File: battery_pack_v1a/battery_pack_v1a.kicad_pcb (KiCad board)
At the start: 4 copper layers, 88 x 94.5 mm, 26 parts, among them J1 Battery Input, Q1 IRF7458, Q2 IRF7458, U1 R5460N208AA

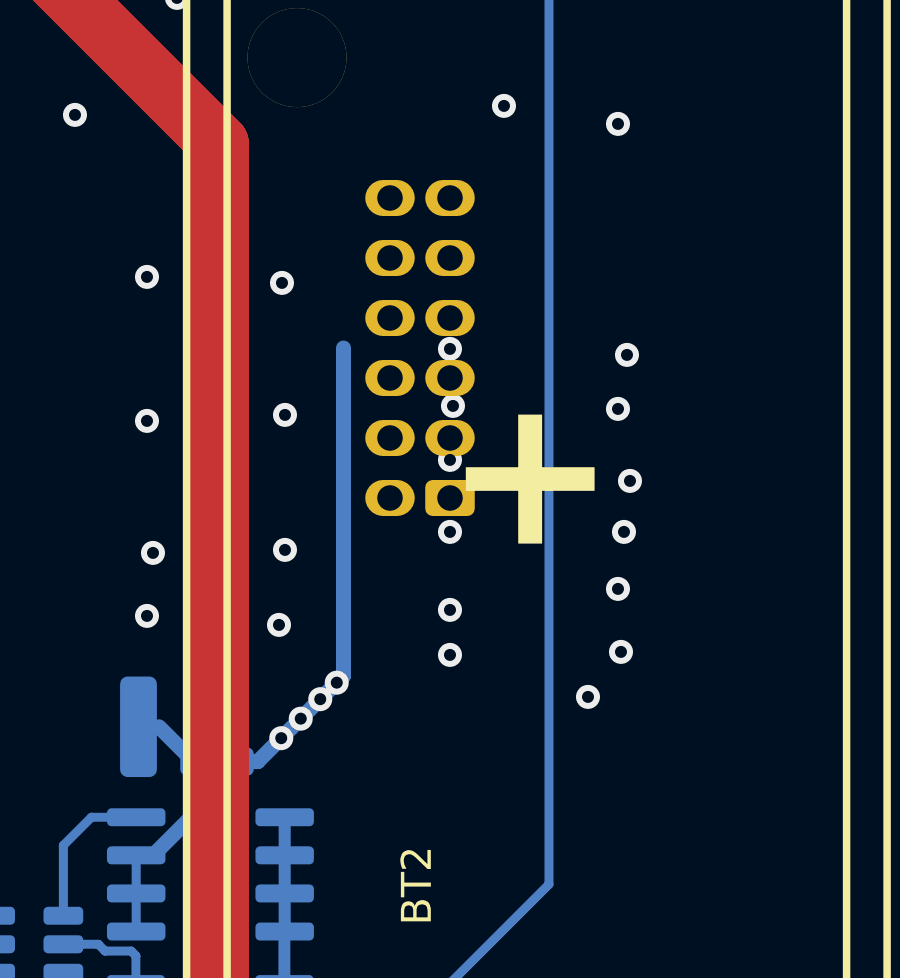
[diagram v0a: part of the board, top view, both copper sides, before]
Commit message: Fixed DF11 footprint and added new (working) repo
Working repo is pack_v1a (ignore pack_v1, will restore original version later in this branch)
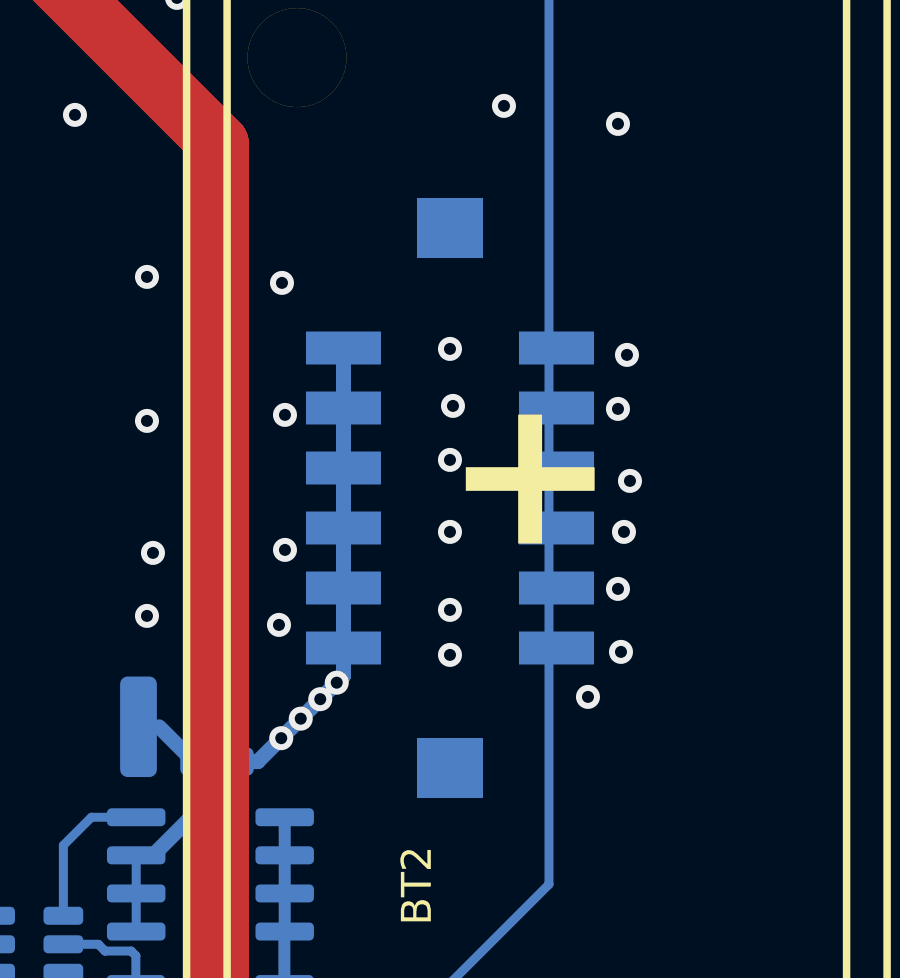
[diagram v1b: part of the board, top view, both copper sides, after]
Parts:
- J1: footprint Connector_Hirose:Hirose_DF11-12DP-2DSA_2x06_P2.00mm_Vertical -> DF11:CONN-SMD_12P-P2.00_DF11CZ-12DP

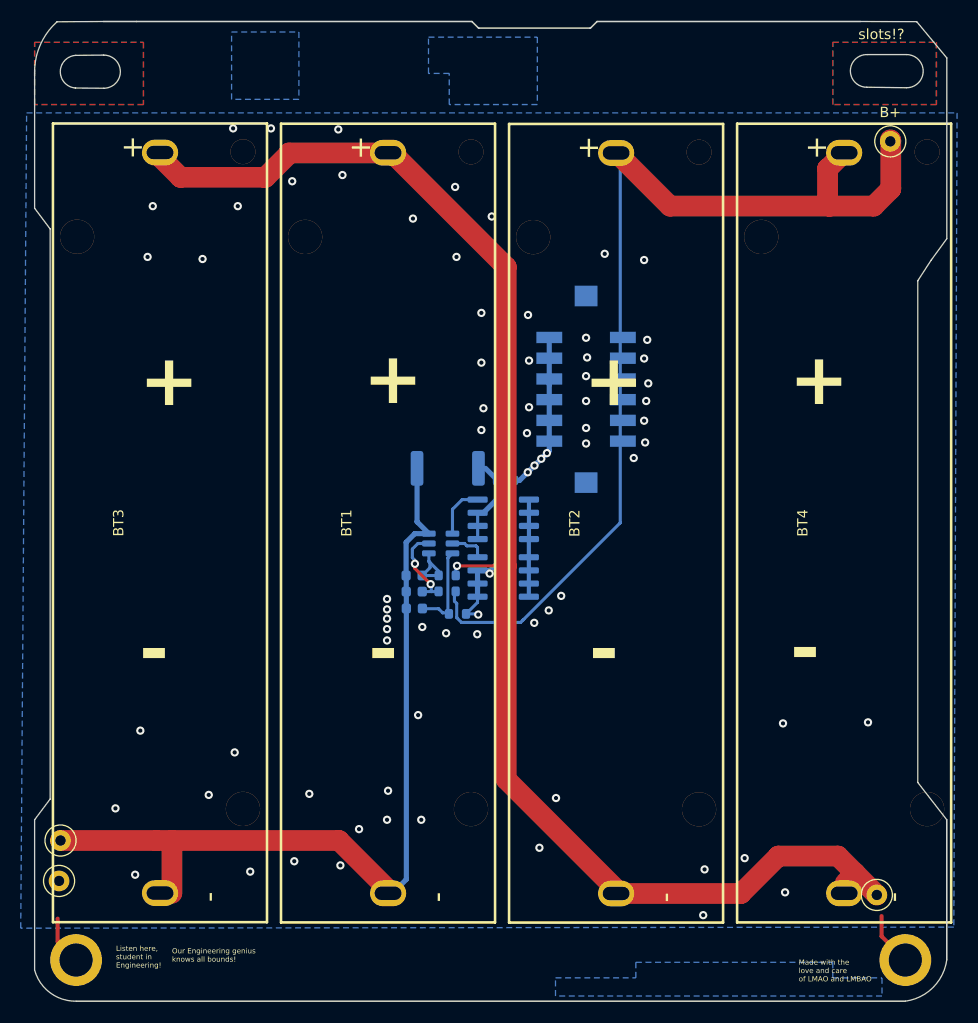
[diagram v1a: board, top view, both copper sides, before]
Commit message: Addressed DRC Errors
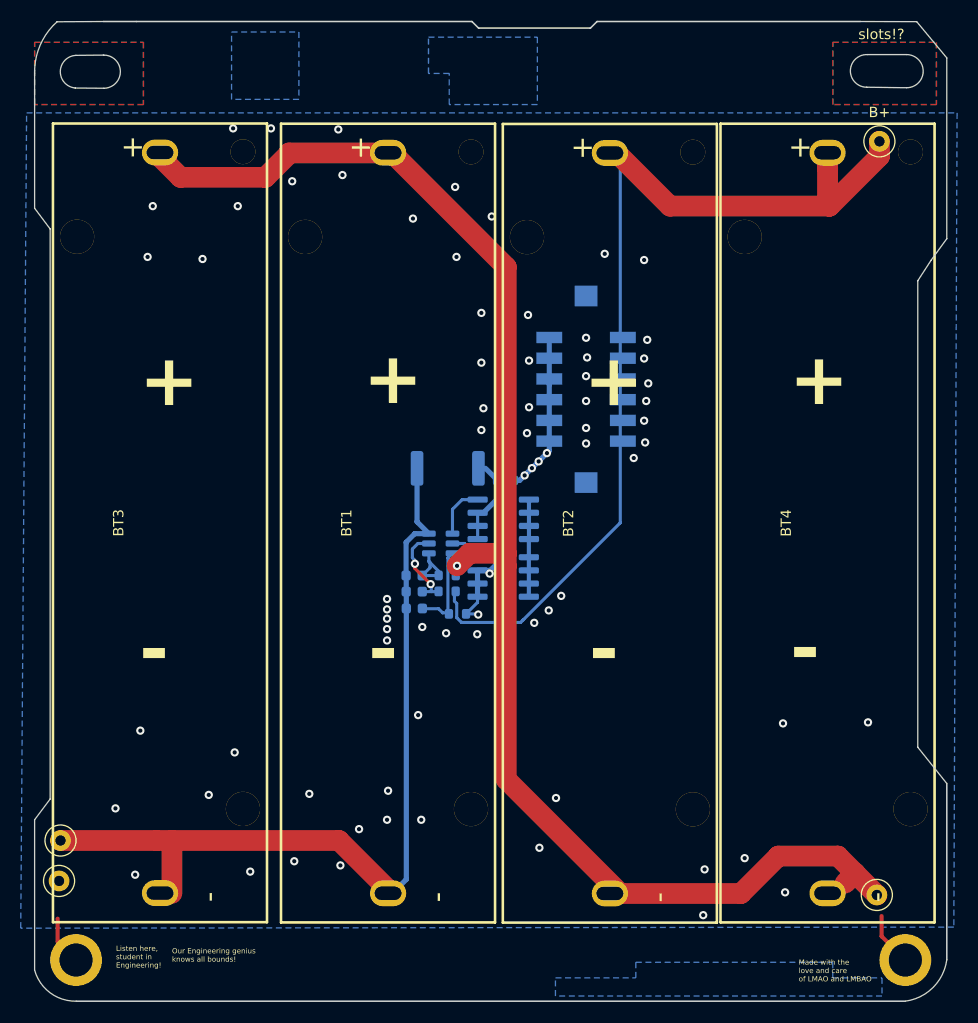
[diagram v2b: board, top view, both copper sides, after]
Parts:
- moved BT4 1.60 mm to (187.0, 89.4)
- moved TP5 1.05 mm to (192.0, 52.5)
- moved BT2 0.60 mm to (166.0, 89.4)
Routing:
- net PACK+: track 98.0 -> 94.3 mm
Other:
- outline, holes or cut-outs redrawn
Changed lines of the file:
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@@
 	(footprint "TestPoint:TestPoint_Loop_D1.80mm_Drill1.0mm_Beaded"
 		(layer "F.Cu")
-		(at 193.05 52.55)
+		(at 192 52.55)
 		(descr "wire loop with bead as test point, loop diameter 1.8mm, hole diameter 1.0mm")
 		(tags "test point wire loop bead")
@@
 	(footprint "Battery Holders:BAT-TH_BH-18650-A6AJ012_MODIFICATION"
 		(layer "F.Cu")
-		(at 166.6 89.39 90)
+		(at 166 89.39 90)
 		(property "Reference" "BT2"
 			(at 0 -4 90)
@@
 	(footprint "Battery Holders:BAT-TH_BH-18650-A6AJ012_MODIFICATION"
 		(layer "F.Cu")
-		(at 188.6 89.37 90)
+		(at 187 89.37 90)
 		(property "Reference" "BT4"
 			(at 0 -4 90)
@@
 	)
 	(gr_line
-		(start 195.7 114.4)
+		(start 195.7 111)
 		(end 195.7 66)
 		(stroke
@@
 	)
 	(gr_line
-		(start 198.5 131.5)
-		(end 198.5 118)
+		(start 198.5 131.499996)
+		(end 198.5 114.5)
 		(stroke
 			(width 0.15)
@@
 	)
 	(gr_line
-		(start 198.5 118)
-		(end 195.7 114.4)
+		(start 198.5 114.5)
+		(end 195.7 111)
 		(stroke
 			(width 0.1)
@@
 	)
 	(via
-		(at 158.075506 84.475506)
+		(at 157.775506 84.775506)
 		(size 0.8)
 		(drill 0.4)
@@
 	)
 	(via
-		(at 158.725506 83.825506)
+		(at 158.475506 84.075506)
 		(size 0.8)
 		(drill 0.4)
@@
 	)
 	(via
-		(at 159.375506 83.175506)
+		(at 159.125506 83.425506)
 		(size 0.8)
 		(drill 0.4)
@@
 	)
 	(segment
+		(start 158.475506 84.075506)
+		(end 159.125506 83.425506)
+		(width 0.5)
+		(layer "B.Cu")
+		(net 6)
+	)
+	(segment
 		(start 153.236 98.136)
 		(end 153.3 98.2)
@@
 	)
 	(segment
-		(start 157.295013 85.255999)
-		(end 158.075506 84.475506)
-		(width 0.5)
-		(layer "B.Cu")
-		(net 6)
-	)
-	(segment
 		(start 153.230098 97.026)
 		(end 153.230098 96.480999)
@@
 	)
 	(segment
-		(start 159.375506 83.175506)
-		(end 159.925506 82.625506)
-		(width 0.5)
-		(layer "B.Cu")
-		(net 6)
-	)
-	(segment
 		(start 156 85.966096)
 		(end 156.710097 85.255999)
@@
 	)
 	(segment
+		(start 157.295013 85.255999)
+		(end 156.710097 85.255999)
+		(width 0.5)
+		(layer "B.Cu")
+		(net 6)
+	)
+	(segment
+		(start 159.125506 83.425506)
+		(end 159.925506 82.625506)
+		(width 0.5)
+		(layer "B.Cu")
+		(net 6)
+	)
+	(segment
 		(start 153.230098 93.940999)
 		(end 154.459001 93.940999)
@@
 	)
 	(segment
-		(start 158.725506 83.825506)
-		(end 159.375506 83.175506)
+		(start 157.775506 84.775506)
+		(end 157.295013 85.255999)
 		(width 0.5)
 		(layer "B.Cu")
@@
 	)
 	(segment
-		(start 158.075506 84.475506)
-		(end 158.725506 83.825506)
+		(start 157.775506 84.775506)
+		(end 158.475506 84.075506)
 		(width 0.5)
 		(layer "B.Cu")
@@
 	)
 	(segment
-		(start 156.710097 85.255999)
-		(end 157.295013 85.255999)
-		(width 0.5)
-		(layer "B.Cu")
-		(net 6)
-	)
-	(segment
 		(start 135.05 53.67)
 		(end 135.05 53.741894)
@@
 	)
 	(segment
+		(start 156 92.3)
+		(end 156 64.67)
+		(width 2)
+		(layer "F.Cu")
+		(net 7)
+	)
+	(segment
 		(start 188.7 124.1)
 		(end 189.65 123.15)
@@
 	)
 	(segment
-		(start 182.25 121.5)
-		(end 188 121.5)
+		(start 156 92.3)
+		(end 152.45 92.3)
 		(width 2)
 		(layer "F.Cu")
@@
 	)
 	(segment
-		(start 167 125.11)
-		(end 178.64 125.11)
+		(start 182.25 121.5)
+		(end 188 121.5)
 		(width 2)
 		(layer "F.Cu")
@@
 	)
 	(segment
-		(start 151.25 93.5)
-		(end 156 93.5)
-		(width 0.3)
+		(start 167 125.11)
+		(end 178.64 125.11)
+		(width 2)
 		(layer "F.Cu")
 		(net 7)
@@
 	(segment
 		(start 156 93.5)
-		(end 156 64.67)
+		(end 156 92.3)
+		(width 2)
+		(layer "F.Cu")
+		(net 7)
+	)
+	(segment
+		(start 152.45 92.3)
+		(end 151.25 93.5)
 		(width 2)
 		(layer "F.Cu")
@@
 	)
 	(segment
-		(start 187.02 55.18)
-		(end 188.5 53.7)
+		(start 187.15 58.8)
+		(end 171.8 58.8)
 		(width 2)
 		(layer "F.Cu")
@@
 	)
 	(segment
-		(start 193.1 52.45)
-		(end 193.05 52.4)
+		(start 187.15 58.8)
+		(end 187.2 58.8)
 		(width 2)
 		(layer "F.Cu")
@@
 	)
 	(segment
-		(start 187.15 58.8)
-		(end 171.8 58.8)
+		(start 187 55.18)
+		(end 187 53.65)
 		(width 2)
 		(layer "F.Cu")
@@
 	)
 	(segment
-		(start 187.15 58.8)
-		(end 191.45 58.8)
+		(start 187.2 58.8)
+		(end 192 54)
 		(width 2)
 		(layer "F.Cu")
@@
 	)
 	(segment
-		(start 193.1 57.15)
-		(end 193.1 52.45)
+		(start 192 54)
+		(end 192 52.55)
 		(width 2)
 		(layer "F.Cu")
@@
 		(width 2)
 		(layer "F.Cu")
-		(net 8)
-	)
-	(segment
-		(start 191.45 58.8)
-		(end 193.1 57.15)
-		(width 2)
-		(layer "F.Cu")

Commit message: Nudged Around Some Trace
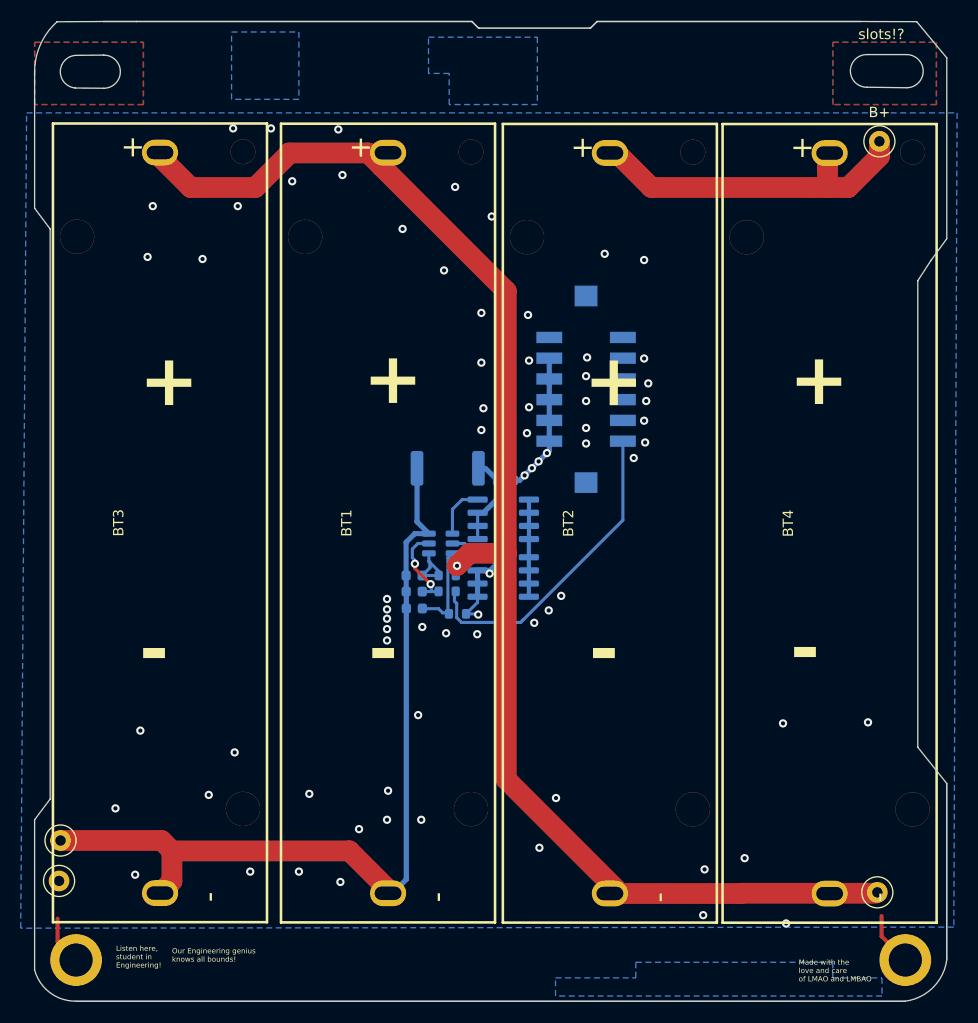
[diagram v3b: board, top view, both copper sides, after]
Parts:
- moved TP3 0.25 mm to (191.8, 125.0)
- moved BT4 0.20 mm to (187.2, 89.4)
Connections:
- J1 pad 11: PACK- -> unconnected-(J1-Pin_11-Pad11)
- J1 pad 12: PACK+ -> unconnected-(J1-Pin_12-Pad12)
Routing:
- net PACK+: track 94.3 -> 63.2 mm
- net BM: track 140.4 -> 136.9 mm
- net PACK-: track 34.1 -> 32.1 mm, vias 75 -> 73
- net B-: track 82.6 -> 82.1 mm

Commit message: Generated Production Files
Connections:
- J1 pad 10: PACK+ -> unconnected-(J1-Pin_10-Pad10)
- J1 pad 9: PACK- -> unconnected-(J1-Pin_9-Pad9)
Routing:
- net PACK-: track 32.1 -> 29.6 mm
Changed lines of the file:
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@@
 	(net 13 "unconnected-(J1-Pin_12-Pad12)")
 	(net 14 "unconnected-(J1-Pin_11-Pad11)")
+	(net 15 "unconnected-(J1-Pin_9-Pad9)")
+	(net 16 "unconnected-(J1-Pin_10-Pad10)")
 	(footprint ""
 		(locked yes)
@@
 			)
 		)
+		(property "LCSC" "C19184084"
+			(at 0 0 0)
+			(layer "F.SilkS")
+			(hide yes)
+			(effects
+				(font
+					(size 1.27 1.27)
+					(thickness 0.15)
+				)
+			)
+		)
 		(sheetname "/")
 		(sheetfile "battery_pack_v1a.kicad_sch")
@@
 			)
 		)
+		(property "LCSC" "C19184084"
+			(at 0 0 0)
+			(layer "F.SilkS")
+			(hide yes)
+			(effects
+				(font
+					(size 1.27 1.27)
+					(thickness 0.15)
+				)
+			)
+		)
 		(sheetname "/")
 		(sheetfile "battery_pack_v1a.kicad_sch")
@@
 			)
 		)
+		(property "LCSC" "C19184084"
+			(at 0 0 0)
+			(layer "F.SilkS")
+			(hide yes)
+			(effects
+				(font
+					(size 1.27 1.27)
+					(thickness 0.15)
+				)
+			)
+		)
 		(sheetname "/")
 		(sheetfile "battery_pack_v1a.kicad_sch")
@@
 			)
 		)
+		(property "LCSC" "C19184084"
+			(at 0 0 0)
+			(layer "F.SilkS")
+			(hide yes)
+			(effects
+				(font
+					(size 1.27 1.27)
+					(thickness 0.15)
+				)
+			)
+		)
 		(sheetname "/")
 		(sheetfile "battery_pack_v1a.kicad_sch")
@@
 			(size 1.1 2.5)
 			(layers "B.Cu" "B.Mask" "B.Paste")
-			(net 6 "PACK-")
+			(net 15 "unconnected-(J1-Pin_9-Pad9)")
 			(pinfunction "Pin_9")
-			(pintype "passive")
+			(pintype "passive+no_connect")
 		)
 		(pad "10" smd rect
@@
 			(size 1.1 2.5)
 			(layers "B.Cu" "B.Mask" "B.Paste")
-			(net 8 "PACK+")
+			(net 16 "unconnected-(J1-Pin_10-Pad10)")
 			(pinfunction "Pin_10")
-			(pintype "passive")
+			(pintype "passive+no_connect")
 		)
 		(pad "11" smd rect
@@
 			(net 14 "unconnected-(J1-Pin_11-Pad11)")
 			(pinfunction "Pin_11")
-			(pintype "passive")
+			(pintype "passive+no_connect")
 		)
 		(pad "12" smd rect
@@
 			(net 13 "unconnected-(J1-Pin_12-Pad12)")
 			(pinfunction "Pin_12")
-			(pintype "passive")
+			(pintype "passive+no_connect")
 		)
 		(pad "13" smd rect
@@
 		(width 0.5)
 		(layer "B.Cu")
-		(net 6)
-	)
-	(segment
-		(start 160.150506 76)
-		(end 160.150506 73.46967)
-		(width 0.5)
-		(layer "B.Cu")
